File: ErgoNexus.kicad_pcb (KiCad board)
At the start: 2 copper layers, 172.1 x 137.2 mm, 110 parts, among them J7 Conn_01x02, J8 Conn_01x02, SW1 SW_Push, SW2 RotaryEncoder_Switch, SW3 SW_Push, SW4 RotaryEncoder_Switch, U1 SuperMini nRF52840, U2 SuperMini nRF52840

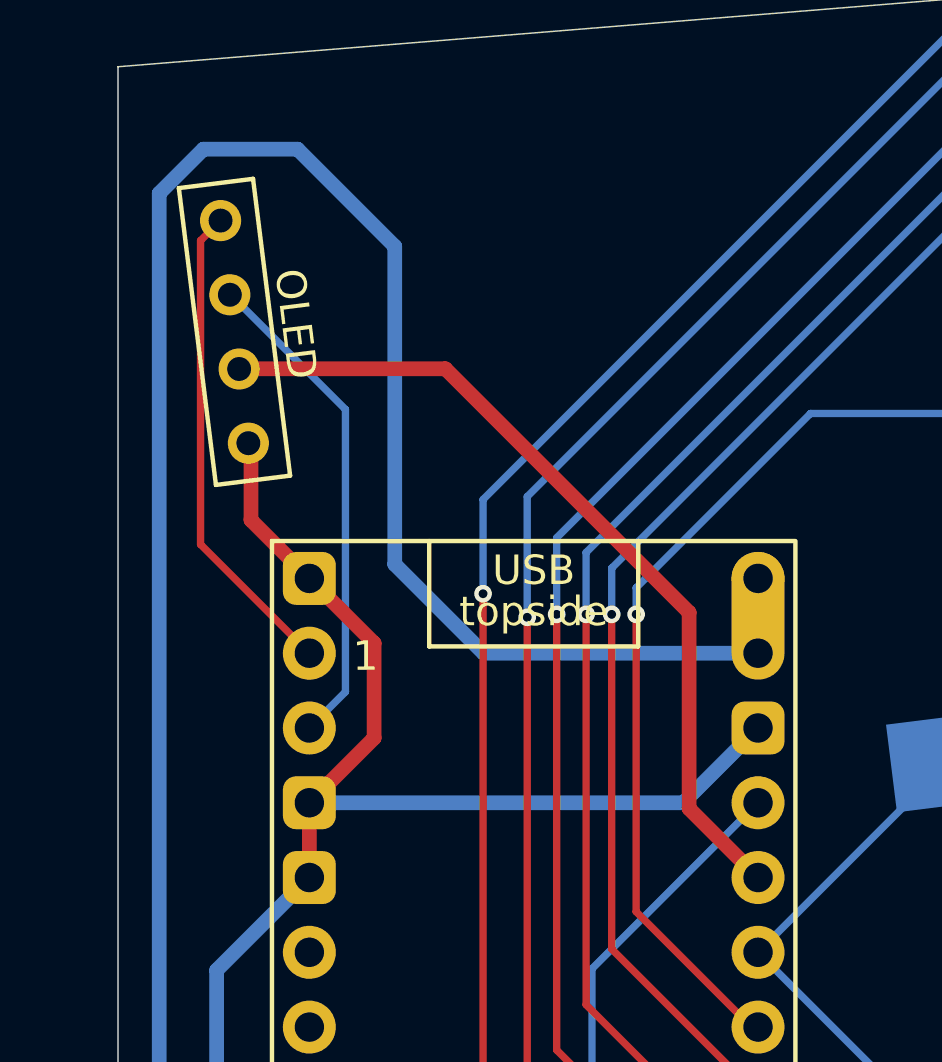
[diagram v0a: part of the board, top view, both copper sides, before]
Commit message: fix: change oled rotation
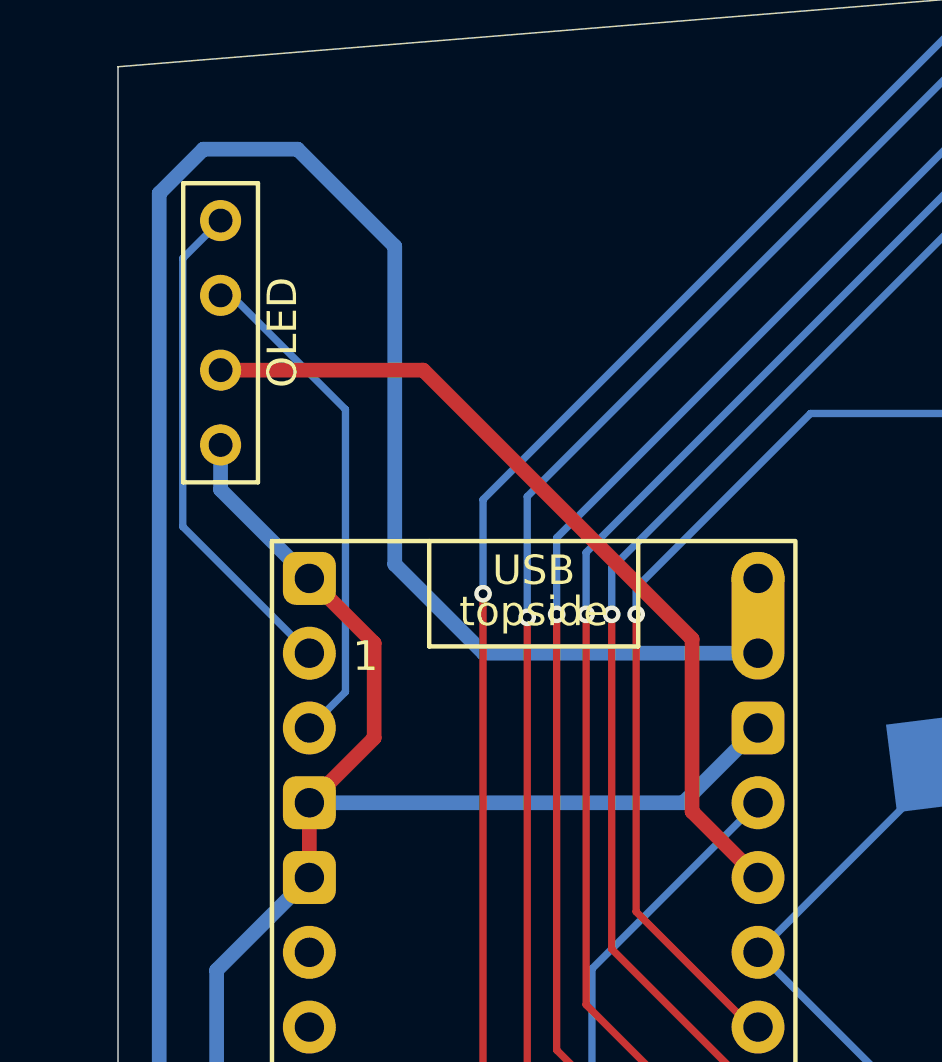
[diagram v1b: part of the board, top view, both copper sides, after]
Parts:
- turned OL8 to -90 degrees
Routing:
- net SDA_R: track 16.5 -> 17.0 mm
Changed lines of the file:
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@@
 	(footprint "kbd_Parts:OLED"
 		(layer "F.Cu")
-		(at 229.869242 73.604737 -82.88)
+		(at 229.869242 73.604737 -90)
 		(descr "Connecteur 6 pins")
 		(tags "CONN DEV")
 		(property "Reference" "OL8"
-			(at 3.699999 2.1 97.12)
+			(at 3.699999 2.1 90)
 			(layer "F.Fab")
 			(effects
@@
 		)
 		(property "Value" "OLED"
-			(at 3.600001 3.300001 97.12)
+			(at 3.600001 3.300001 90)
 			(layer "F.SilkS")
 			(hide yes)
@@
 		)
 		(property "Datasheet" ""
-			(at 0 0 97.12)
+			(at 0 0 90)
 			(layer "F.Fab")
 			(hide yes)
@@
 		)
 		(property "Description" ""
-			(at 0 0 97.12)
+			(at 0 0 90)
 			(layer "F.Fab")
 			(hide yes)
@@
 		)
 		(fp_text user "OLED"
-			(at 3.800001 -2.1 97.12)
+			(at 3.800001 -2.1 90)
 			(layer "F.SilkS")
 			(effects
@@
 		)
 		(pad "1" thru_hole circle
-			(at 0 0 277.12)
+			(at 0 0 270)
 			(size 1.397 1.397)
 			(drill 0.8128)
@@
 		)
 		(pad "2" thru_hole circle
-			(at 2.540001 0.000001 277.12)
+			(at 2.540001 0.000001 270)
 			(size 1.397 1.397)
 			(drill 0.8128)
@@
 		)
 		(pad "3" thru_hole circle
-			(at 5.08 0 277.12)
+			(at 5.08 0 270)
 			(size 1.397 1.397)
 			(drill 0.8128)
@@
 		)
 		(pad "4" thru_hole circle
-			(at 7.620001 0.000001 277.12)
+			(at 7.620001 0.000001 270)
 			(size 1.397 1.397)
 			(drill 0.8128)
@@
 	)
 	(segment
-		(start 245.785 86.917591)
-		(end 237.505386 78.637977)
+		(start 229.869242 78.684737)
+		(end 236.752146 78.684737)
 		(width 0.5)
 		(layer "F.Cu")
@@
 	)
 	(segment
-		(start 245.785 93.579666)
-		(end 245.785 86.917591)
+		(start 245.885 93.679666)
+		(end 248.125 95.919666)
 		(width 0.5)
 		(layer "F.Cu")
@@
 	)
 	(segment
-		(start 237.505386 78.637977)
-		(end 230.55692 78.637977)
+		(start 245.885 87.817591)
+		(end 245.885 93.679666)
 		(width 0.5)
 		(layer "F.Cu")
@@
 	)
 	(segment
-		(start 248.125 95.919666)
-		(end 245.785 93.579666)
+		(start 236.752146 78.684737)
+		(end 245.885 87.817591)
 		(width 0.5)
 		(layer "F.Cu")
@@
 	)
 	(segment
-		(start 230.900759 83.775425)
-		(end 232.885 85.759666)
-		(width 0.5)
-		(layer "F.Cu")
-		(net 98)
-	)
-	(segment
 		(start 232.885 93.379666)
 		(end 235.085 91.179666)
@@
 	)
 	(segment
-		(start 230.900759 81.154597)
-		(end 230.900759 83.775425)
-		(width 0.5)
-		(layer "F.Cu")
-		(net 98)
-	)
-	(segment
 		(start 237.285 153.879666)
 		(end 237.785 153.379666)
@@
 	)
 	(segment
+		(start 229.869241 82.743907)
+		(end 232.885 85.759666)
+		(width 0.5)
+		(layer "B.Cu")
+		(net 98)
+	)
+	(segment
 		(start 247.824014 140.618679)
 		(end 250.324014 138.118679)
@@
 	)
 	(segment
+		(start 229.869241 81.224738)
+		(end 229.869241 82.743907)
+		(width 0.5)
+		(layer "B.Cu")
+		(net 98)
+	)
+	(segment
 		(start 237.785 153.379666)
 		(end 237.785 142.579666)
@@
 	)
 	(segment
-		(start 232.885 88.299666)
-		(end 229.188581 84.603247)
+		(start 228.585 83.999666)
+		(end 232.885 88.299666)
 		(width 0.25)
-		(layer "F.Cu")
+		(layer "B.Cu")
 		(net 100)
 	)
 	(segment
-		(start 229.188581 74.285398)
-		(end 229.869242 73.604737)
+		(start 228.585 74.888979)
+		(end 228.585 83.999666)
 		(width 0.25)
-		(layer "F.Cu")
+		(layer "B.Cu")
 		(net 100)
 	)
 	(segment
-		(start 229.188581 84.603247)
-		(end 229.188581 74.285398)
+		(start 229.869242 73.604737)
+		(end 228.585 74.888979)
 		(width 0.25)
-		(layer "F.Cu")
+		(layer "B.Cu")
 		(net 100)
 	)

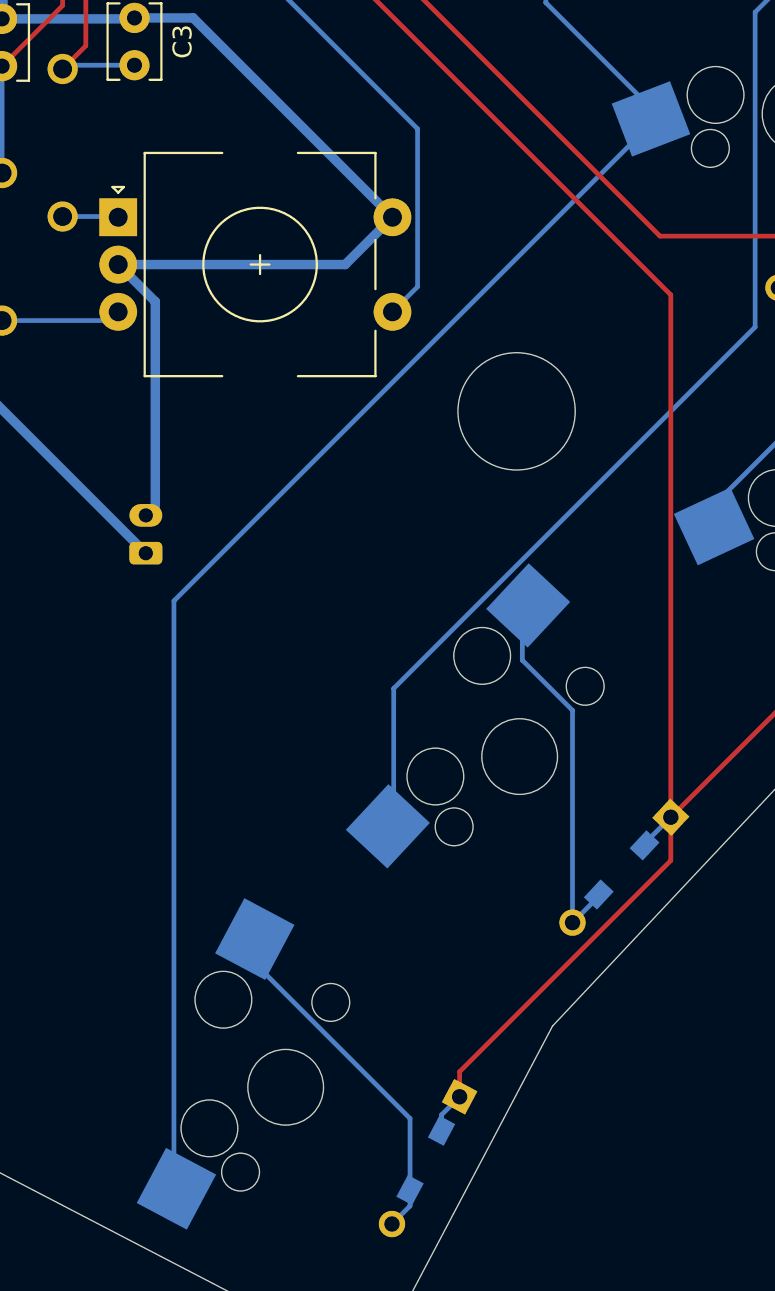
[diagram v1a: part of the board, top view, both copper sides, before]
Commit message: fix: battery connector position
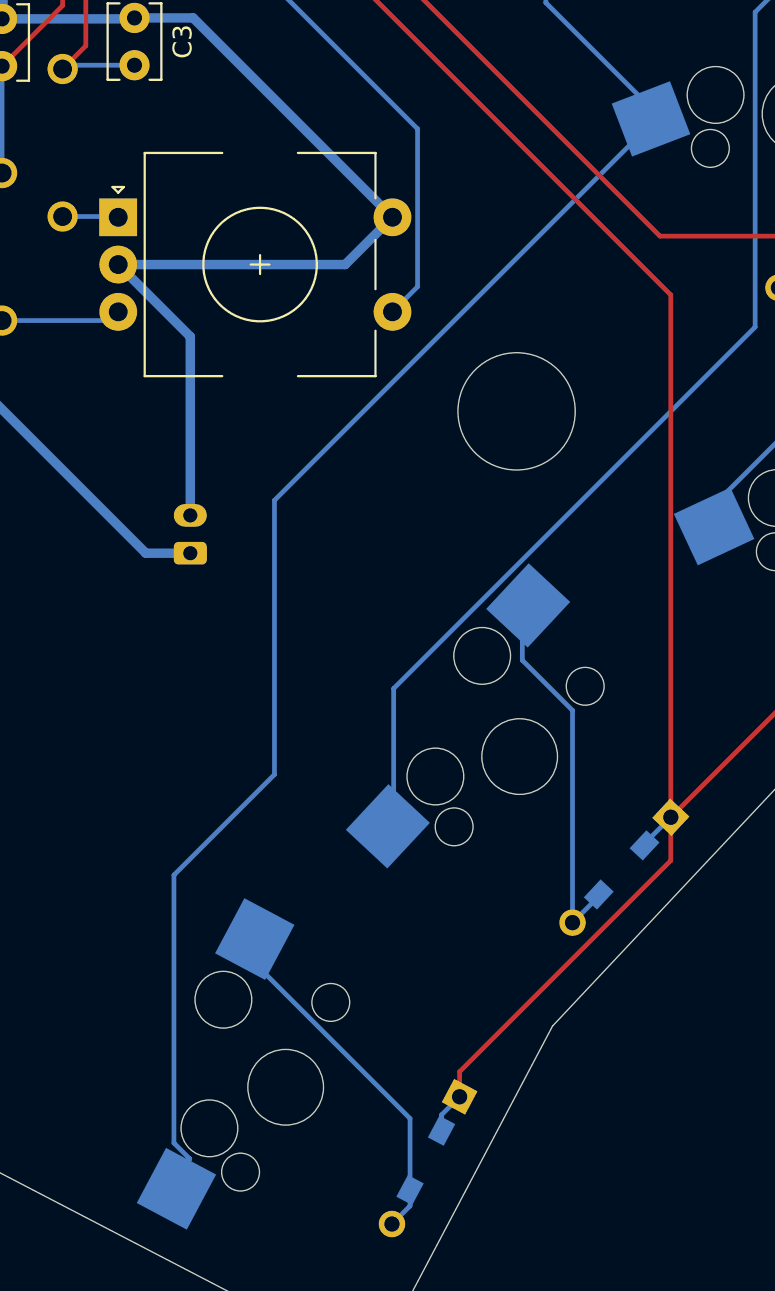
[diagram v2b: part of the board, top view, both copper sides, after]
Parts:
- moved J7 2.35 mm to (239.6, 155.9)
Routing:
- net BAT_R: track 121.5 -> 123.9 mm
- net Col1_R: track 116.8 -> 117.5 mm
- net GND_R: track 121.9 -> 122.5 mm
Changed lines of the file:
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@@
 	(footprint "Connector_JST:JST_PH_S2B-PH-K_1x02_P2.00mm_Horizontal"
 		(layer "B.Cu")
-		(at 237.285 155.879666 90)
+		(at 239.635 155.879666 90)
 		(descr "JST PH series connector, S2B-PH-K (http://www.jst-mfg.com/product/pdf/eng/ePH.pdf), generated with kicad-footprint-generator")
 		(tags "connector JST PH top entry")
@@
 	)
 	(segment
-		(start 264.411892 132.757136)
-		(end 238.770167 158.398861)
+		(start 238.770167 187.061854)
+		(end 239.609012 187.9007)
 		(width 0.25)
 		(layer "B.Cu")
@@
 	)
 	(segment
-		(start 238.770167 158.398861)
+		(start 264.411892 132.757136)
+		(end 244.085 153.084028)
+		(width 0.25)
+		(layer "B.Cu")
+		(net 75)
+	)
+	(segment
+		(start 239.609012 187.9007)
 		(end 238.770167 188.739545)
+		(width 0.25)
+		(layer "B.Cu")
+		(net 75)
+	)
+	(segment
+		(start 244.085 153.084028)
+		(end 244.085 167.579666)
 		(width 0.25)
 		(layer "B.Cu")
@@
 	)
 	(segment
+		(start 244.085 167.579666)
+		(end 238.770167 172.894499)
+		(width 0.25)
+		(layer "B.Cu")
+		(net 75)
+	)
+	(segment
 		(start 258.430863 108.765529)
 		(end 248.125 98.459666)
@@
 		(start 258.430863 112.610449)
 		(end 258.430863 108.765529)
+		(width 0.25)
+		(layer "B.Cu")
+		(net 75)
+	)
+	(segment
+		(start 238.770167 172.894499)
+		(end 238.770167 187.061854)
 		(width 0.25)
 		(layer "B.Cu")
@@
 	)
 	(segment
+		(start 232.485 71.179666)
+		(end 229.285 71.179666)
+		(width 0.5)
+		(layer "B.Cu")
+		(net 80)
+	)
+	(segment
 		(start 227.785 146.379666)
 		(end 237.285 155.879666)
@@
 	)
 	(segment
-		(start 232.485 71.179666)
-		(end 229.285 71.179666)
-		(width 0.5)
-		(layer "B.Cu")
-		(net 80)
-	)
-	(segment
 		(start 235.785 85.279666)
 		(end 235.785 74.479666)
@@
 		(start 248.125 88.299666)
 		(end 238.805 88.299666)
+		(width 0.5)
+		(layer "B.Cu")
+		(net 80)
+	)
+	(segment
+		(start 237.285 155.879666)
+		(end 239.635 155.879666)
 		(width 0.5)
 		(layer "B.Cu")
@@
 	)
 	(segment
-		(start 237.285 153.879666)
-		(end 237.785 153.379666)
-		(width 0.5)
-		(layer "B.Cu")
-		(net 98)
-	)
-	(segment
 		(start 229.735 99.069666)
 		(end 229.735 123.779666)
@@
 	)
 	(segment
-		(start 237.785 142.579666)
-		(end 235.824013 140.618679)
-		(width 0.5)
-		(layer "B.Cu")
-		(net 98)
-	)
-	(segment
 		(start 239.785001 127.579666)
 		(end 250.324014 138.118679)
@@
 	)
 	(segment
+		(start 239.635 153.879666)
+		(end 239.635 144.429666)
+		(width 0.5)
+		(layer "B.Cu")
+		(net 98)
+	)
+	(segment
 		(start 247.824014 140.618679)
 		(end 250.324014 138.118679)
@@
 	)
 	(segment
+		(start 239.635 144.429666)
+		(end 235.824013 140.618679)
+		(width 0.5)
+		(layer "B.Cu")
+		(net 98)
+	)
+	(segment
 		(start 229.685 127.629666)
 		(end 236.635 127.629666)
@@
 		(width 0.5)
 		(layer "B.Cu")
-		(net 98)
-	)
-	(segment
-		(start 237.785 153.379666)
-		(end 237.785 142.579666)
-		(width 0.5)
-		(layer "B.Cu")

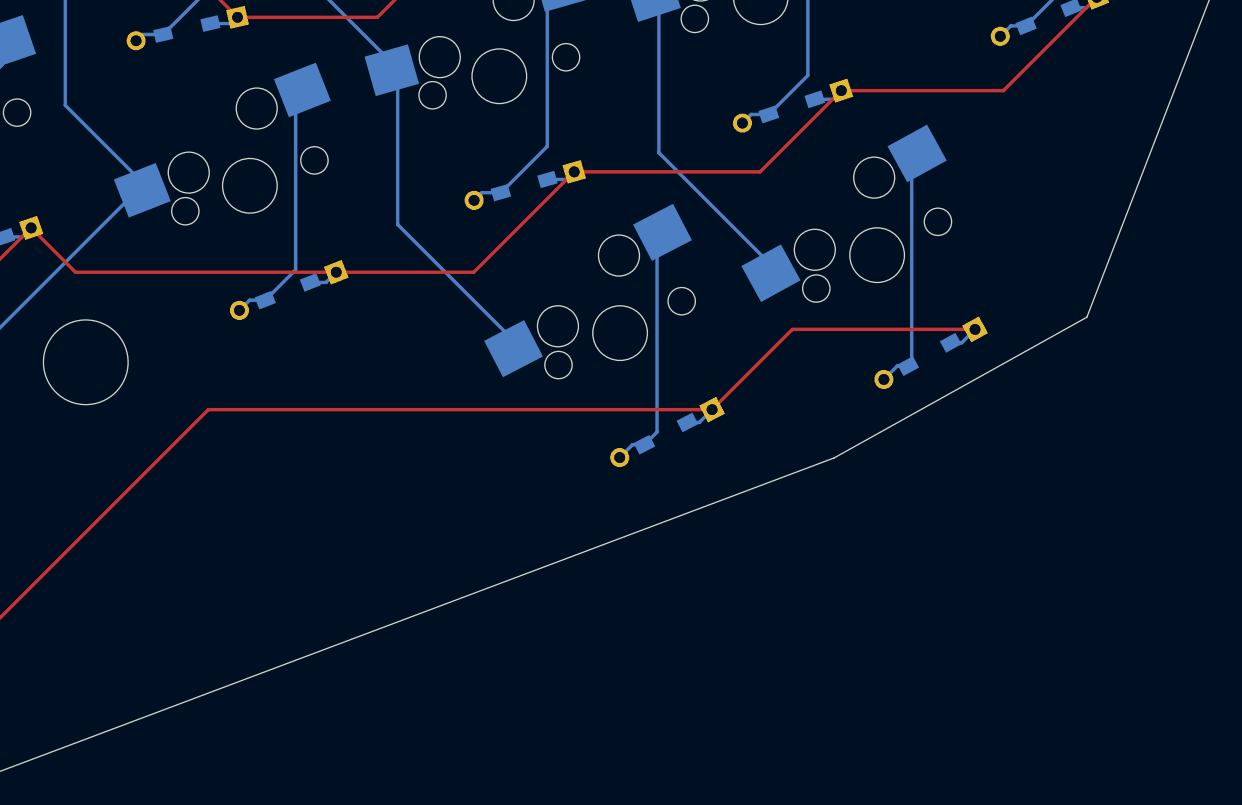
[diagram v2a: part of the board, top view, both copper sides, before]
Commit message: feat: add copy right to front silk
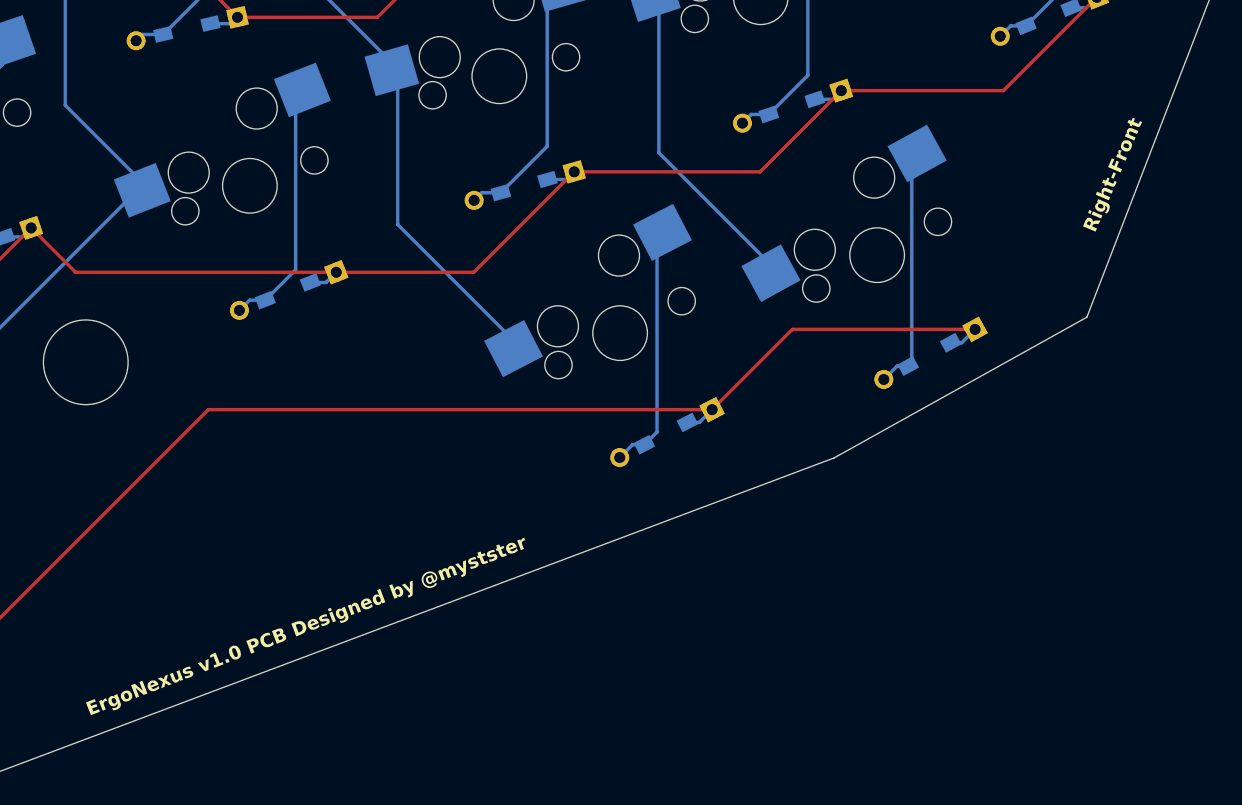
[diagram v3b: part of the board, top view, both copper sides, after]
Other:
- board text added: "ErgoNexus v1.0 PCB Designed by @mystster"
- board text added: "Right-Back"
- board text added: "Right-Front"
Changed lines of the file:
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@@
 		(layer "Margin")
+	)
+	(gr_text "ErgoNexus v1.0 PCB Designed by @mystster"
+		(at 316.185 156.179666 21)
+		(layer "F.SilkS")
+		(effects
+			(font
+				(size 1 1)
+				(thickness 0.2)
+				(bold yes)
+			)
+			(justify left bottom)
+		)
+	)
+	(gr_text "Right-Front"
+		(at 389.885 120.779666 67)
+		(layer "F.SilkS")
+		(effects
+			(font
+				(size 1 1)
+				(thickness 0.2)
+				(bold yes)
+			)
+			(justify left bottom)
+		)
+	)
+	(gr_text "Right-Back"
+		(at 393.385 112.379666 67)
+		(layer "B.SilkS")
+		(effects
+			(font
+				(size 1 1)
+				(thickness 0.2)
+				(bold yes)
+			)
+			(justify left bottom mirror)
+		)
 	)
 	(segment
